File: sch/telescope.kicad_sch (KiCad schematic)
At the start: 57 parts, among them J1 USB_B, J2 M1, J3 M1, J4 12V, Q1 MMBT3904, Q2 MMBT3904, SW1 RST, SW2 IO0, SW3 PWR, U1 A5984GLPTR-T, U2 A5984GLPTR-T, U3 FT260S-U, U4 ESP32-WROOM-32, U5 LC76G, U6 AP62200WU-7

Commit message: pin assignment
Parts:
- added D5: LED, symbol Device:LED
- added R19, R20, R21: 5k, symbol Device:R_US
- added R22: 130, symbol Device:R_US
- added R23: 10k, Resistor_SMD:R_0805_2012Metric_Pad1.20x1.40mm_HandSolder, symbol Device:R_US
- J3: value M1 -> M2
- R5, R6: footprint Resistor_SMD:R_0805_2012Metric_Pad1.20x1.40mm_HandSolder -> (none)
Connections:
- net +3V3: now also R19.1, R21.1, R23.2
- net ESP_IO0: now also R23.1
- net GND: now also R20.2, R22.2
- net GPS_FIX: now also U4.30 (IO18)
- net GPS_RX: now also U4.28 (IO17)
- net GPS_TX: now also U4.27 (IO16)
- net M1_DIR: now also U4.14 (IO12), R20.1
- net M1_MS1: now also U4.33 (IO21)
- net M1_MS2: now also U4.36 (IO22)
- net M1_MS3: now also U4.37 (IO23)
- net M1_STEP: now also U4.13 (IO14)
- net M2_DIR: now also U4.16 (IO13)
- net M2_MS1: now also U4.11 (IO26)
- net M2_MS2: now also U4.12 (IO27)
- net M2_MS3: now also U4.8 (IO32)
- net M2_STEP: now also U4.23 (IO15), R21.2
- net M_SLEEP: now also R5.2, U4.26 (IO4)
- net ~{M_ENA}: now also U4.31 (IO19)
- net M1_nFAULT: now reaches U1.4 (nFAULT)
- net M1_nFAULT: now also R6.2, U4.6 (IO34); no longer R5.2
- net M2_nFAULT: now reaches U2.4 (nFAULT)
- net M2_nFAULT: now also U4.7 (IO35), R19.2; no longer R6.2
- net ~{M1_RST}: now reaches U4.10 (IO25)
- net ~{M1_RST}: now also U1.7 (~{RESET})
- net LED: now reaches U4.24 (IO2)
- net LED: now also D5.2 (A)
- net ~{M2_RST}: now reaches U4.9 (IO33)
- net ~{M2_RST}: now also U2.7 (~{RESET})
- removed net ~{M_RST}: U1.7 (~{RESET}), U2.7 (~{RESET})
- new net: D5.1 (K), R22.1
- no-connect marks 22 -> 28
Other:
- note added: "DTR RTS -> EN IO0 1 1 1 1 0 0 1 1 1 0 0 1 0 1 1 0"
- moved on the sheet: AE1, C10, C11, C12, C13, C14, D4, Q1, Q2, R11, R13, R14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

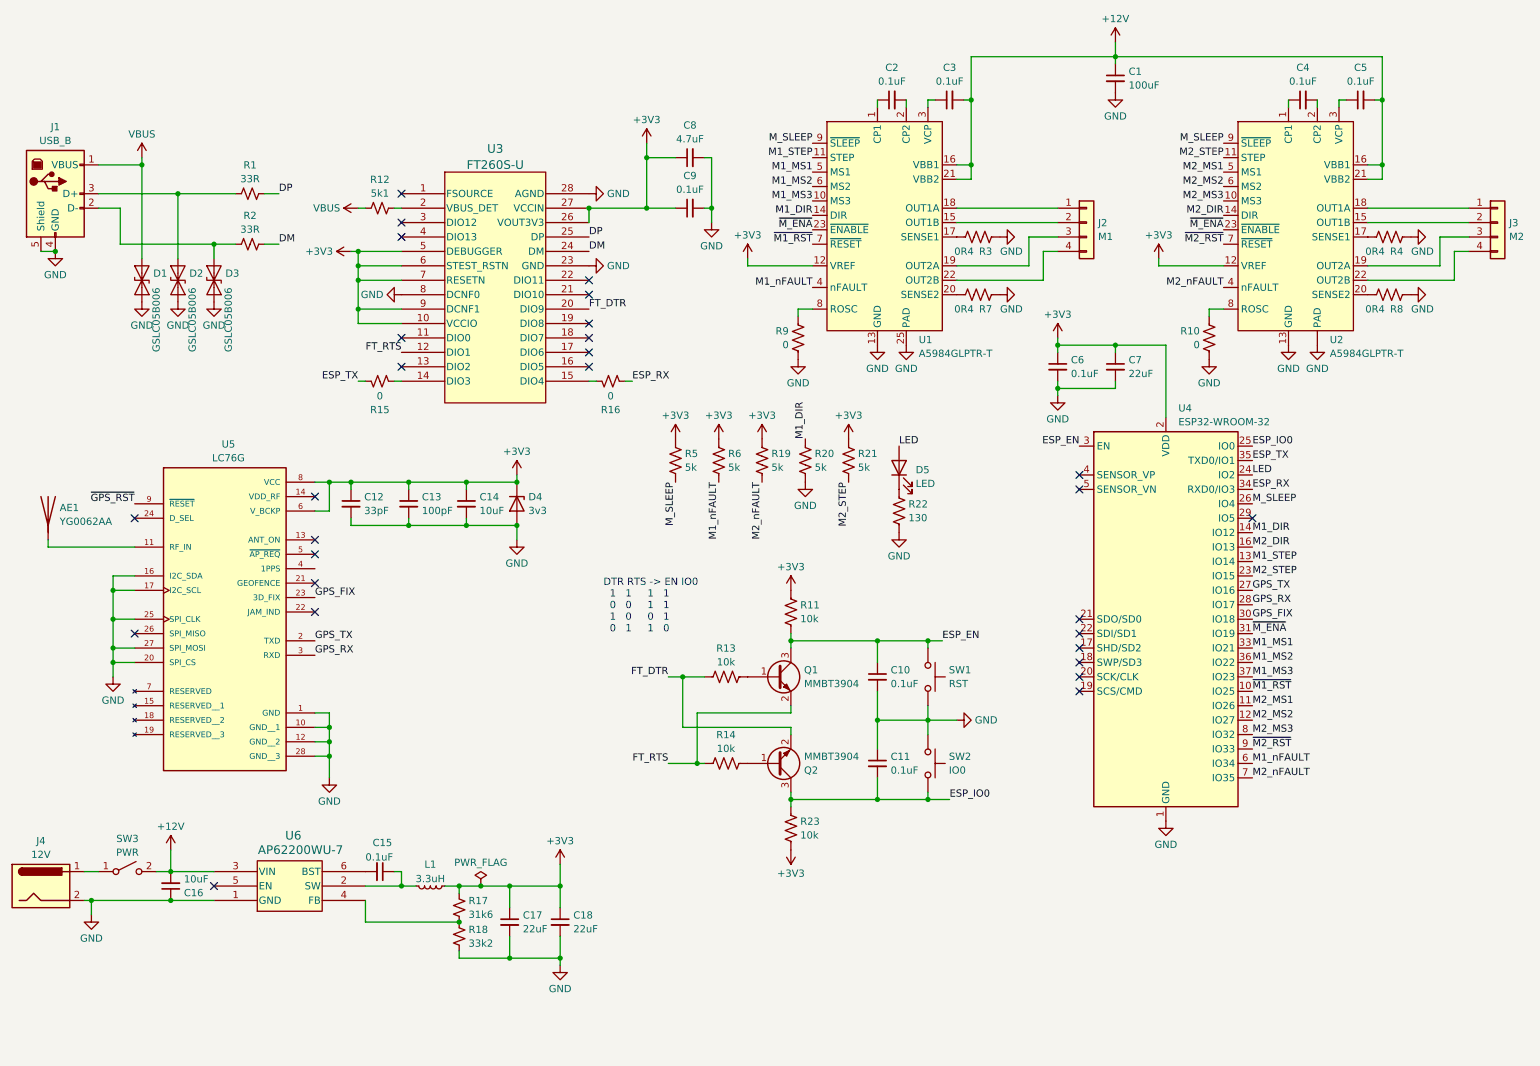
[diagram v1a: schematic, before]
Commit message: add isense and vsense, start layout
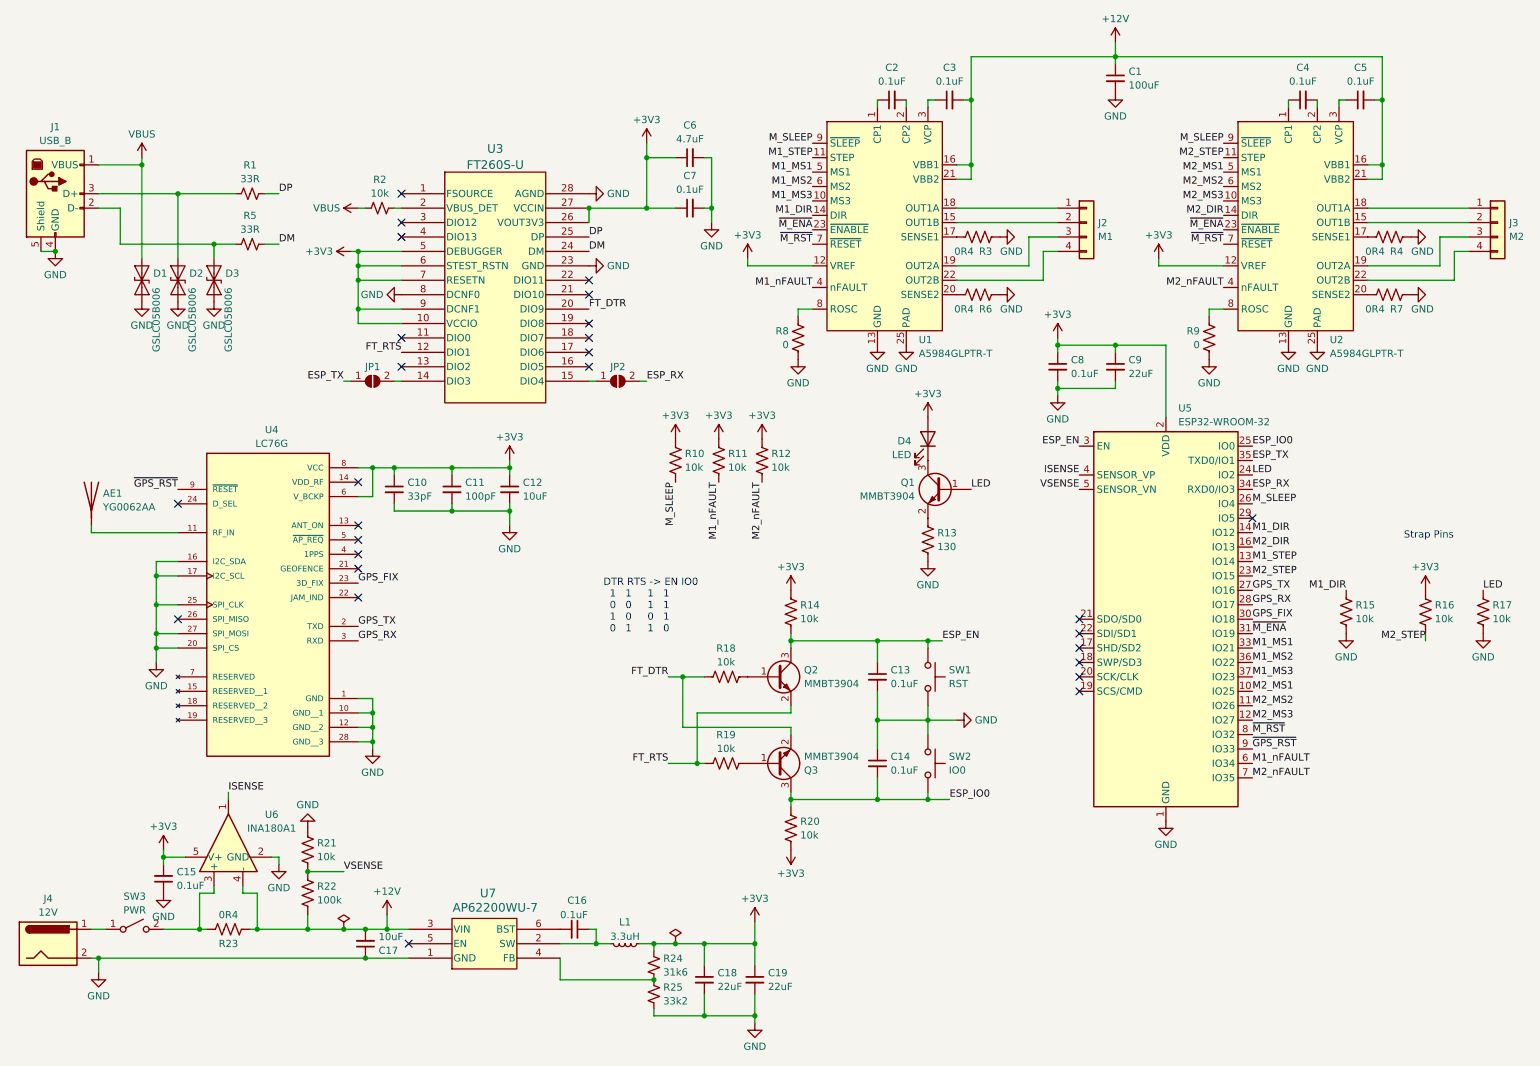
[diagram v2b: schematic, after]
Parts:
- removed D4: 3v3, symbol Device:D_Zener
- removed R15, R16: 0, Resistor_SMD:R_0805_2012Metric_Pad1.20x1.40mm_HandSolder, symbol Device:R_Small_US
- added C15: 0.1uF, Capacitor_SMD:C_0805_2012Metric_Pad1.18x1.45mm_HandSolder, symbol Device:C_Small
- added JP1, JP2: SolderJumper_2_Open, Jumper:SolderJumper-2_P1.3mm_Open_TrianglePad1.0x1.5mm, symbol Jumper:SolderJumper_2_Open
- added Q1: MMBT3904, Package_TO_SOT_SMD:SOT-23, symbol Transistor_BJT:MMBT3904
- added R17, R21: 10k, Resistor_SMD:R_0805_2012Metric_Pad1.20x1.40mm_HandSolder, symbol Device:R_US
- added R22: 100k, Resistor_SMD:R_0805_2012Metric_Pad1.20x1.40mm_HandSolder, symbol Device:R_US
- added R23: 0R4, Resistor_SMD:R_2512_6332Metric_Pad1.40x3.35mm_HandSolder, symbol Device:R_US
- added U6: INA180A1, Package_TO_SOT_SMD:SOT-23-5, symbol Amplifier_Current:INA180A1
- AE1: now left out of the parts list
- C10: renamed from C12; now left out of the parts list
- C11: renamed from C13; now left out of the parts list
- C12: renamed from C14; now left out of the parts list
- D1, D2, D3: footprint Diode_SMD:D_SOD-323 -> Diode_SMD:D_SOD-323_HandSoldering
- D4: renamed from D5; footprint (none) -> LED_SMD:LED_1206_3216Metric_Pad1.42x1.75mm_HandSolder
- J1: footprint (none) -> Connector_USB:USB_B_OST_USB-B1HSxx_Horizontal
- J2, J3: footprint (none) -> Connector_JST:JST_PH_B4B-PH-K_1x04_P2.00mm_Vertical
- J4: footprint (none) -> PJ-037B:CUI_PJ-037B
- R10: renamed from R5; value 5k -> 10k; footprint (none) -> Resistor_SMD:R_0805_2012Metric_Pad1.20x1.40mm_HandSolder
- R11: renamed from R6; value 5k -> 10k; footprint (none) -> Resistor_SMD:R_0805_2012Metric_Pad1.20x1.40mm_HandSolder
- R12: renamed from R19; value 5k -> 10k; footprint (none) -> Resistor_SMD:R_0805_2012Metric_Pad1.20x1.40mm_HandSolder
- R13: renamed from R22; footprint (none) -> Resistor_SMD:R_0805_2012Metric_Pad1.20x1.40mm_HandSolder
- R15: renamed from R20; value 5k -> 10k; footprint (none) -> Resistor_SMD:R_0805_2012Metric_Pad1.20x1.40mm_HandSolder
- R16: renamed from R21; value 5k -> 10k; footprint (none) -> Resistor_SMD:R_0805_2012Metric_Pad1.20x1.40mm_HandSolder
- R2: renamed from R12; value 5k1 -> 10k
- SW1, SW2: footprint (none) -> Button_Switch_SMD:SW_Push_1P1T_NO_6x6mm_H9.5mm
- SW3: footprint (none) -> R13-66:R13-66
- U1, U2: symbol telescope:A5984 -> A5984:A5984
- U4: renamed from U5; now left out of the parts list
- renumbered C10 to C13, C11 to C14, C15 to C16, C16 to C17, C17 to C18, C18 to C19, C8 to C6, C9 to C7, C6 to C8, C7 to C9, Q1 to Q2, Q2 to Q3, R11 to R14, R13 to R18, R14 to R19, R23 to R20, R17 to R24, R18 to R25, R2 to R5, R7 to R6, R8 to R7, R9 to R8, R10 to R9, U4 to U5, U6 to U7
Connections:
- net +12V: now also R22.2, R23.2, U6.4 (-); no longer SW3.2 (B)
- net +3V3: now also D4.2 (A), C15.2, U6.5 (V+)
- net ESP_RX: now also JP2.2 (B)
- net ESP_TX: now also JP1.1 (A)
- net GND: now also U2.25 (PAD), C15.1, R17.2, R21.1, U6.2 (GND); no longer U2. (PAD)
- net LED: now also Q1.1 (B), R17.1; no longer D4.2 (A)
- net M2_MS1: now also U5.10 (IO25); no longer U5.11 (IO26)
- net M2_MS2: now also U5.11 (IO26); no longer U5.12 (IO27)
- net M2_MS3: now also U5.12 (IO27); no longer U5.8 (IO32)
- net ~{GPS_RST}: now also U5.9 (IO33)
- net at R13.1: now also Q1.2 (E); no longer D4.1 (K)
- net at U3.15 (DIO4): now also JP2.1 (A)
- net ISENSE: now reaches U5.4 (SENSOR_VP)
- net ISENSE: now also U6.1
- net VSENSE: now reaches U5.5 (SENSOR_VN)
- net VSENSE: now also R21.2, R22.1
- net at U3.14 (DIO3): now also JP1.2 (B)
- net ~{M1_RST} renamed ~{M_RST}
- net ~{M_RST}: now also U2.7 (~{RESET}), U5.8 (IO32); no longer U5.10 (IO25)
- removed net ~{M2_RST}: U2.7 (~{RESET}), U5.9 (IO33)
- new net: D4.1 (K), Q1.3 (C)
- new net: R23.1, SW3.2 (B), U6.3 (+)
- no-connect marks 28 -> 27
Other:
- note added: "Strap Pins"
- moved on the sheet: AE1, C10, C11, C12, C16, C17, C18, C19, D4, J4, L1, R13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

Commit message: layout, route, and add digikey numbers
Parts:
- added H1, H2, H3: MountingHole_Pad, MountingHole:MountingHole_3.2mm_M3_Pad, symbol Mechanical:MountingHole_Pad
- added J5: UART, Connector_PinHeader_2.54mm:PinHeader_1x04_P2.54mm_Vertical, symbol Connector:Conn_01x04_Pin
- C13, C14, C15, C16, C2, C3, C4, C5, C7, C8: Digikey PN (none) -> 311-1140-1-ND
- C18, C19, C9: Digikey PN (none) -> 1276-6687-1-ND
- C6: Digikey PN (none) -> 1276-1244-1-ND
- D1, D2, D3: Digikey PN (none) -> 4786-GSLC05B006CT-ND
- D4: Digikey PN (none) -> 3147-T1341USD-30C000112U1930CT-ND
- J1: Digikey PN (none) -> ED2982-ND
- J2, J3: footprint Connector_JST:JST_PH_B4B-PH-K_1x04_P2.00mm_Vertical -> Connector_JST:JST_PH_S4B-PH-K_1x04_P2.00mm_Horizontal; Digikey PN (none) -> JST Sales America Inc.
- J4: Digikey PN (none) -> CP-037B-ND
- R1, R5: Digikey PN (none) -> RMCF0805JT33R0CT-ND
- R23: footprint Resistor_SMD:R_2512_6332Metric_Pad1.40x3.35mm_HandSolder -> Resistor_SMD:R_1206_3216Metric_Pad1.30x1.75mm_HandSolder; Digikey PN (none) -> 283-MFHA1206R4000FCCT-ND
- R24: Digikey PN (none) -> 311-31.6KCRCT-ND
- R25: Digikey PN (none) -> RMCF0805FT33K2CT-ND
- R3, R4, R6, R7: footprint Resistor_SMD:R_0805_2012Metric_Pad1.20x1.40mm_HandSolder -> Resistor_SMD:R_1206_3216Metric_Pad1.30x1.75mm_HandSolder; Digikey PN (none) -> 283-MFHA1206R4000FCCT-ND
- R8, R9: Digikey PN (none) -> 311-0.0ARCT-ND
- SW1, SW2: footprint Button_Switch_SMD:SW_Push_1P1T_NO_6x6mm_H9.5mm -> TS04-66-43-BK-160:SW_TS04-66-43-BK-160-SMT; Digikey PN (none) -> TS04-66-43-BK-160-SMT
- U1, U2: Digikey PN (none) -> 620-1787-1-ND
- U3: Digikey PN (none) -> 768-1282-5-ND
- U6: Digikey PN (none) -> 296-47652-1-ND
- renumbered R16 to R26
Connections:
- net +3V3: now also J5.1 (Pin_1)
- net ESP_RX: now also J5.3 (Pin_3)
- net ESP_TX: now also JP1.2 (B), J5.2 (Pin_2); no longer JP1.1 (A)
- net GND: now also H1.1, H2.1, H3.1, J5.4 (Pin_4)
- net at U1.15 (OUT1B): now also J2.3 (Pin_3); no longer J2.2 (Pin_2)
- net at U1.18 (OUT1A): now also J2.4 (Pin_4); no longer J2.1 (Pin_1)
- net at U1.19 (OUT2A): now also J2.2 (Pin_2); no longer J2.3 (Pin_3)
- net at U1.22 (OUT2B): now also J2.1 (Pin_1); no longer J2.4 (Pin_4)
- net at U3.14 (DIO3): now also JP1.1 (A); no longer JP1.2 (B)
- net at J3.1 (Pin_1): now also U2.22 (OUT2B); no longer U2.18 (OUT1A)
- net at J3.2 (Pin_2): now also U2.19 (OUT2A); no longer U2.15 (OUT1B)
- net at J3.3 (Pin_3): now also U2.15 (OUT1B); no longer U2.19 (OUT2A)
- net at J3.4 (Pin_4): now also U2.18 (OUT1A); no longer U2.22 (OUT2B)

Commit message: fix digikey part numbers
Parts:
- J2, J3: Digikey PN JST Sales America Inc. -> 455-1721-ND
- SW1, SW2: Digikey PN TS04-66-43-BK-160-SMT -> 2223-TS04-66-43-BK-160-SMT-ND
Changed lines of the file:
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@@
       (effects (font (size 1.27 1.27)) hide)
     )
-    (property "Digikey PN" "JST Sales America Inc." (at 207.01 53.34 0)
+    (property "Digikey PN" "455-1721-ND" (at 207.01 53.34 0)
       (effects (font (size 1.27 1.27)) hide)
     )
@@
       (effects (font (size 1.27 1.27)) hide)
     )
-    (property "Digikey PN" "TS04-66-43-BK-160-SMT" (at 179.07 146.05 0)
+    (property "Digikey PN" "2223-TS04-66-43-BK-160-SMT-ND" (at 179.07 146.05 0)
       (effects (font (size 1.27 1.27)) hide)
     )
@@
       (effects (font (size 1.27 1.27)) hide)
     )
-    (property "Digikey PN" "JST Sales America Inc." (at 279.4 53.34 0)
+    (property "Digikey PN" "455-1721-ND" (at 279.4 53.34 0)
       (effects (font (size 1.27 1.27)) hide)
     )
@@
       (effects (font (size 1.27 1.27)) hide)
     )
-    (property "Digikey PN" "TS04-66-43-BK-160-SMT" (at 179.07 130.81 0)
-      (effects (font (size 1.27 1.27)) hide)
-    )
+    (property "Digikey PN" "2223-TS04-66-43-BK-160-SMT-ND" (at 179.07 130.81 0)
+      (effects (font (size 1.27 1.27)) hide)
+    )

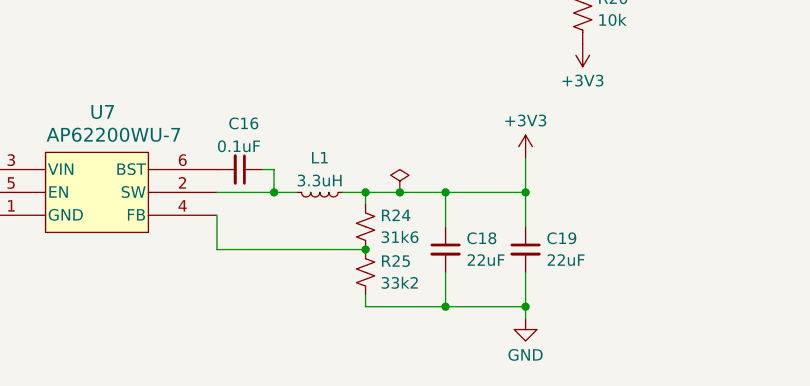
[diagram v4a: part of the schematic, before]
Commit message: fix feedback resistor value
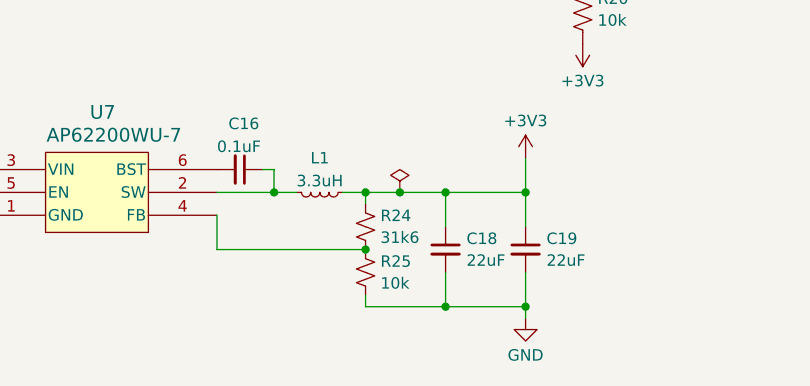
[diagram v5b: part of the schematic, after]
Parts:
- R25: value 33k2 -> 10k
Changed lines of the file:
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@@
       (effects (font (size 1.27 1.27)) (justify left))
     )
-    (property "Value" "33k2" (at 132.461 187.9021 0)
+    (property "Value" "10k" (at 132.461 187.9021 0)
       (effects (font (size 1.27 1.27)) (justify left))
     )

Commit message: add series resistor to led bjt
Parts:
- added R16: 10k, Resistor_SMD:R_0805_2012Metric_Pad1.20x1.40mm_HandSolder, symbol Device:R_US
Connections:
- net LED: now also R16.2; no longer Q1.1 (B)
- new net: Q1.1 (B), R16.1
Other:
- moved on the sheet: D4, Q1, R13

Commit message: increase reset capacitor value
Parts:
- C13: value 0.1uF -> 1uF
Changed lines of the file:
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@@
 		(fields_autoplaced yes)
 		(property "Reference" "C13"
-			(at 172.5041 129.6042 0)
+			(at 172.5041 129.6041 0)
 			(effects
 				(font
@@
 			)
 		)
-		(property "Value" "0.1uF"
+		(property "Value" "1uF"
 			(at 172.5041 132.0284 0)
 			(effects

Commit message: pull down bootstrap pin for serial logging
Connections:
- net +3V3: no longer R26.1
- net GND: now also R26.1
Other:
- moved on the sheet: R26
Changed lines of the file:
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@@
 	(wire
 		(pts
-			(xy 266.7 123.19) (xy 266.7 124.46)
-		)
-		(stroke
-			(width 0)
-			(type default)
-		)
-	)
-	(wire
-		(pts
 			(xy 135.89 130.81) (xy 139.7 130.81)
 		)
@@
 	)
 	(label "M2_STEP"
-		(at 266.7 124.46 180)
+		(at 266.7 115.57 180)
 		(fields_autoplaced yes)
 		(effects
@@
 	(symbol
 		(lib_id "Device:R_US")
-		(at 266.7 119.38 0)
+		(at 266.7 119.38 180)
 		(unit 1)
 		(exclude_from_sim no)
@@
 		(fields_autoplaced yes)
 		(property "Reference" "R26"
-			(at 268.351 118.1679 0)
+			(at 268.351 118.1678 0)
 			(effects
 				(font
 					(size 1.27 1.27)
 				)
-				(justify left)
+				(justify right)
 			)
 		)
@@
 					(size 1.27 1.27)
 				)
-				(justify left)
+				(justify right)
 			)
 		)
 		(property "Footprint" "Resistor_SMD:R_0805_2012Metric_Pad1.20x1.40mm_HandSolder"
-			(at 267.716 119.634 90)
+			(at 265.684 119.126 90)
 			(effects
 				(font
@@
 	)
 	(symbol
+		(lib_id "power:GND")
+		(at 266.7 123.19 0)
+		(unit 1)
+		(exclude_from_sim no)
+		(in_bom yes)
+		(on_board yes)
+		(dnp no)
+		(fields_autoplaced yes)
+		(property "Reference" "#PWR037"
+			(at 266.7 129.54 0)
+			(effects
+				(font
+					(size 1.27 1.27)
+				)
+				(hide yes)
+			)
+		)
+		(property "Value" "GND"
+			(at 266.7 127.3231 0)
+			(effects
+				(font
+					(size 1.27 1.27)
+				)
+			)
+		)
+		(property "Footprint" ""
+			(at 266.7 123.19 0)
+			(effects
+				(font
+					(size 1.27 1.27)
+				)
+				(hide yes)
+			)
+		)
+		(property "Datasheet" ""
+			(at 266.7 123.19 0)
+			(effects
+				(font
+					(size 1.27 1.27)
+				)
+				(hide yes)
+			)
+		)
+		(property "Description" ""
+			(at 266.7 123.19 0)
+			(effects
+				(font
+					(size 1.27 1.27)
+				)
+				(hide yes)
+			)
+		)
+		(pin "1"
+		)
+		(instances
+			(project "telescope"
+				(path "/7a0030c5-5f3a-40ee-8491-a5192f52fe77"
+					(reference "#PWR037")
+					(unit 1)
+				)
+			)
+		)
+	)
+	(symbol
 		(lib_id "Transistor_BJT:MMBT3904")
 		(at 152.4 130.81 0)
@@
 					(unit 1)
 				)
-			)
-		)
-	)
-	(symbol
-		(lib_id "power:+3V3")
-		(at 266.7 115.57 0)
-		(unit 1)
-		(exclude_from_sim no)
-		(in_bom yes)
-		(on_board yes)
-		(dnp no)
-		(fields_autoplaced yes)
-		(property "Reference" "#PWR037"
-			(at 266.7 119.38 0)
-			(effects
-				(font
-					(size 1.27 1.27)
-				)
-				(hide yes)
-			)
-		)
-		(property "Value" "+3V3"
-			(at 266.7 111.4369 0)
-			(effects
-				(font
-					(size 1.27 1.27)
-				)
-			)
-		)
-		(property "Footprint" ""
-			(at 266.7 115.57 0)
-			(effects
-				(font
-					(size 1.27 1.27)
-				)
-				(hide yes)
-			)
-		)
-		(property "Datasheet" ""
-			(at 266.7 115.57 0)
-			(effects
-				(font
-					(size 1.27 1.27)
-				)
-				(hide yes)
-			)
-		)
-		(property "Description" ""
-			(at 266.7 115.57 0)
-			(effects
-				(font
-					(size 1.27 1.27)
-				)
-				(hide yes)
-			)
-		)
-		(pin "1"
-		)
-		(instances
-			(project "telescope"
-				(path "/7a0030c5-5f3a-40ee-8491-a5192f52fe77"
-					(reference "#PWR037")
-					(unit 1)
-				)
